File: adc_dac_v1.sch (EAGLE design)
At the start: 275 parts, among them IC1 OPA1662, IC2 ADA4610-2, IC3 ADA4610-2, IC4 OPA1662, J1 PJ-202AH, J2 PJ-002B, J3 2-406541-3, P1 M-2X06-87759_M, P2 M-2X10-87759_M, U1 AD7960BCPZ-RL7, U10 UA78M05CDCYR, U11 LP5907MFX-1.8/NOPB, U12 ADP2300AUJZ-R7, U13 LM317LIPKG3, U14 LM317LIPKG3, U15 LM337LMX/NOPB, U16 ADR395AUJZ-REEL7, U17 MAX5802, U18 LM337LMX/NOPB, U19 MAX6070BAUT21+T, U2 AD5453, U20 CD40106BM96, U21 ADA4932-1YCPZ-R7, U22 AD7960BCPZ-RL7, U23 BC857BS-13-F, U24 BC857BS-13-F, U25 ADA4932-1YCPZ-R7, U26 AD7960BCPZ-RL7, U27 ADA4932-1YCPZ-R7, U28 AD7960BCPZ-RL7, U29 AD5453, U3 ADA4932-1YCPZ-R7, U31 BC857BS-13-F, U4 NLSX3018DTR2G, U5 NLSX3018DTR2G, U6 ADS7952SRHBT, U7 OPA202, U8 REF5025AIDR, U9 ADP150AUJZ-3.3-R7, X1 BU-SMA-G, X2 BU-SMA-G, X3 BU-SMA-G, X4 BU-SMA-G, X5 BU-SMA-G, X6 BU-SMA-G, X7 BU-SMA-G, X8 BU-SMA-G, X9 1365-10

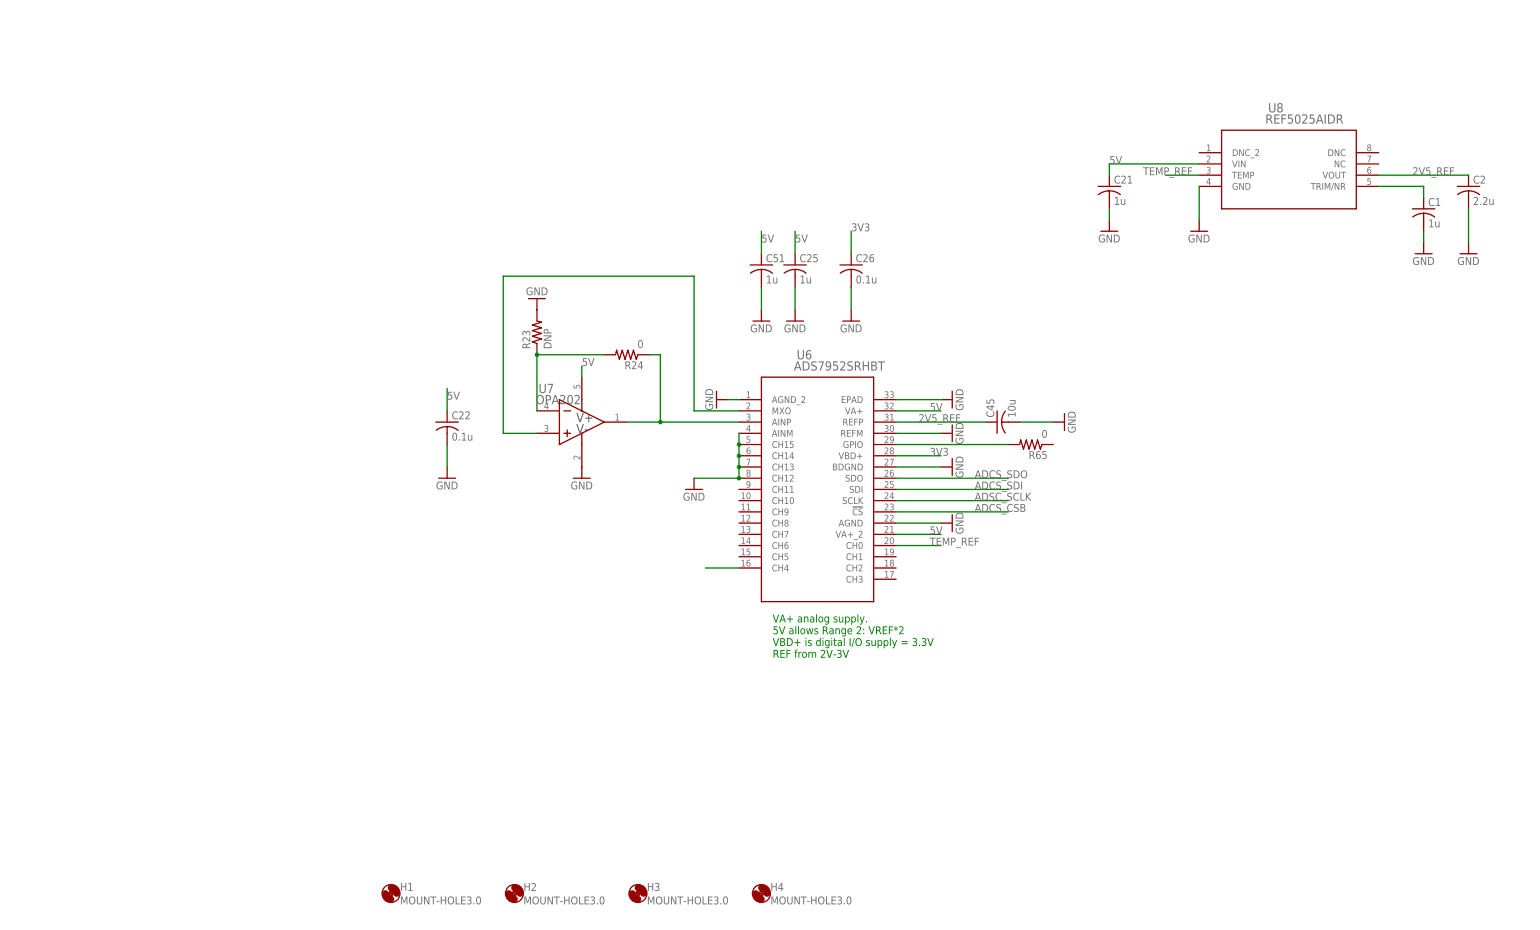
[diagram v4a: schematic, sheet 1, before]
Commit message: x4 copies of the fast DAC in layout
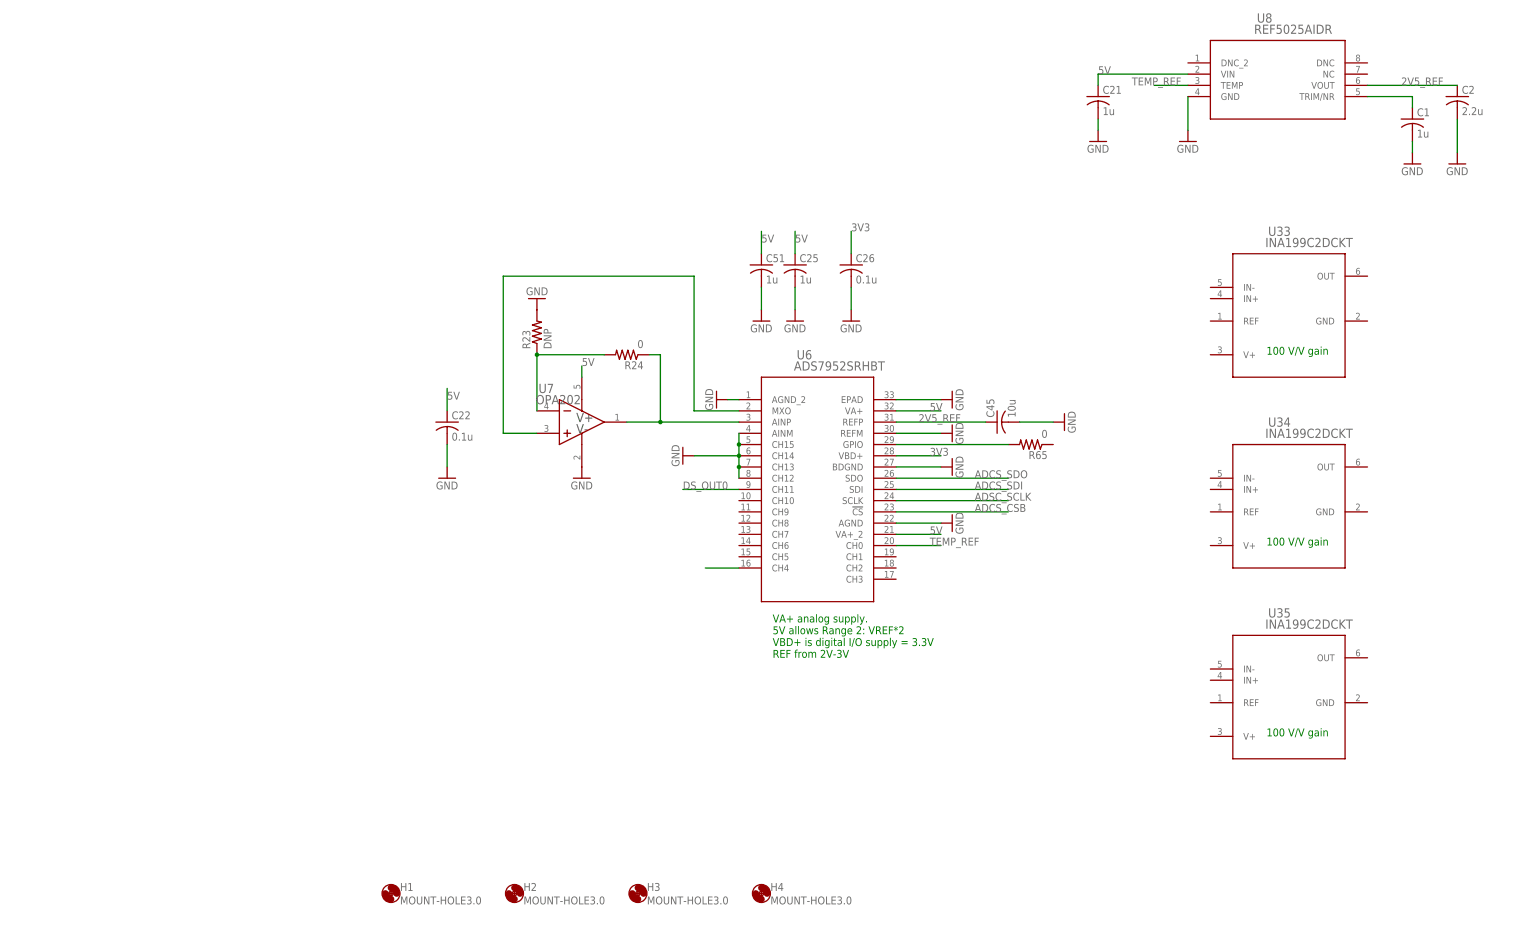
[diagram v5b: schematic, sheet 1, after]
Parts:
- added C105, C107, C113, C115: DNP, rcl:C-USC0603
- added C106, C108, C109, C111, C112, C114, C116, C117, C119, C120: 0.1u, rcl:C-USC0603
- added C110, C118: 2p, rcl:C-USC0603
- added IC5, IC7: ADA4610-2, analog-devices:ADA4692-2R
- added IC6, IC8: OPA1662, open_covg:OPA1662
- added R112, R113, R117, R122, R123, R127: 0, rcl:R-US_R0603
- added R114, R124: 10k, rcl:R-US_R0603
- added R115, R116, R125, R126: 20k, rcl:R-US_R0603
- added R118, R119, R121, R128, R129, R131: 1k, rcl:R-US_R0603
- added R120, R130: 2k, rcl:R-US_R0603
- added U30, U32: AD5453, open_covg:AD5453YRMZ-REEL7
- added U33, U34, U35: INA199C2DCKT, open_covg:INA199C2DCKT
- U29: value AD5453 -> AD5453YRMZ-REEL7
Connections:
- new net D2_CSB: U30.SYNCB
- new net D2_IOUT: C110.1, IC6B.IN+, U30.IOUT1
- new net D2_OUT: C107.1, J3.4, R113.2
- new net D2_SCLK: U30.SCLK
- new net D2_SDI: U30.SDIN
- new net D2_VREF_BUF: C105.1, R112.2, R116.1, U30.VREF
- new net D3_CSB: U32.SYNCB
- new net D3_IOUT: C118.1, IC8B.IN+, U32.IOUT1
- new net D3_OUT: C115.1, J3.7, R123.2
- new net D3_SCLK: U32.SCLK
- new net D3_SDI: U32.SDIN
- new net D3_VREF_BUF: C113.1, R122.2, R126.1, U32.VREF
- new net N$10D2: IC5B.IN-, R120.2, R121.1
- new net N$10D3: IC7B.IN-, R130.2, R131.1
- new net N$25D2: IC6A.OUT, R112.1, R118.2
- new net N$25D3: IC8A.OUT, R122.1, R128.2
- new net N$2D2: C110.2, R117.1, U30.RFB
- new net N$2D3: C118.2, R127.1, U32.RFB
- new net N$3D2: IC5A.IN+, R114.2, R115.1, R116.2
- new net N$3D3: IC7A.IN+, R124.2, R125.1, R126.2
- new net N$4D2: IC6B.OUT, R114.1, R117.2
- new net N$4D3: IC8B.OUT, R124.1, R127.2
- new net N$5D2: IC5A.OUT, IC5B.IN+, R115.2
- new net N$5D3: IC7A.OUT, IC7B.IN+, R125.2
- new net N$7D2: IC6A.IN-, R118.1, R119.2
- new net N$7D3: IC8A.IN-, R128.1, R129.2
- new net N$8D2: IC5B.OUT, R113.1, R120.1
- new net N$8D3: IC7B.OUT, R123.1, R130.1
- net +15V: now also C108.1, C112.1, C116.1, C120.1, IC5P.V+, IC6P.V+, IC7P.V+, IC8P.V+
- net -15V: now also C109.1, C111.1, C117.1, C119.1, IC5P.V-, IC6P.V-, IC7P.V-, IC8P.V-
- net 3V3: now also C106.1, C114.1, U30.VDD, U32.VDD
- net 5V_REF: now also IC6A.IN+, IC8A.IN+
- net D1_OUT: now also J3.3
- net DS_OUT0: now also U6.CH11
- net GND: now also C105.2, C106.2, C107.2, C108.2, C109.2, C111.2, C112.2, C113.2, C114.2, C115.2, C116.2, C117.2, C119.2, C120.2, IC5A.IN-, IC6B.IN-, IC7A.IN-, IC8B.IN-, J3.5, J3.6, J3.8, R119.1, R121.2, R129.1, R131.2, U30.GND, U32.GND
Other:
- note added: "100 V/V gain"
- moved on the sheet: C1, C2, C21, J3, U8

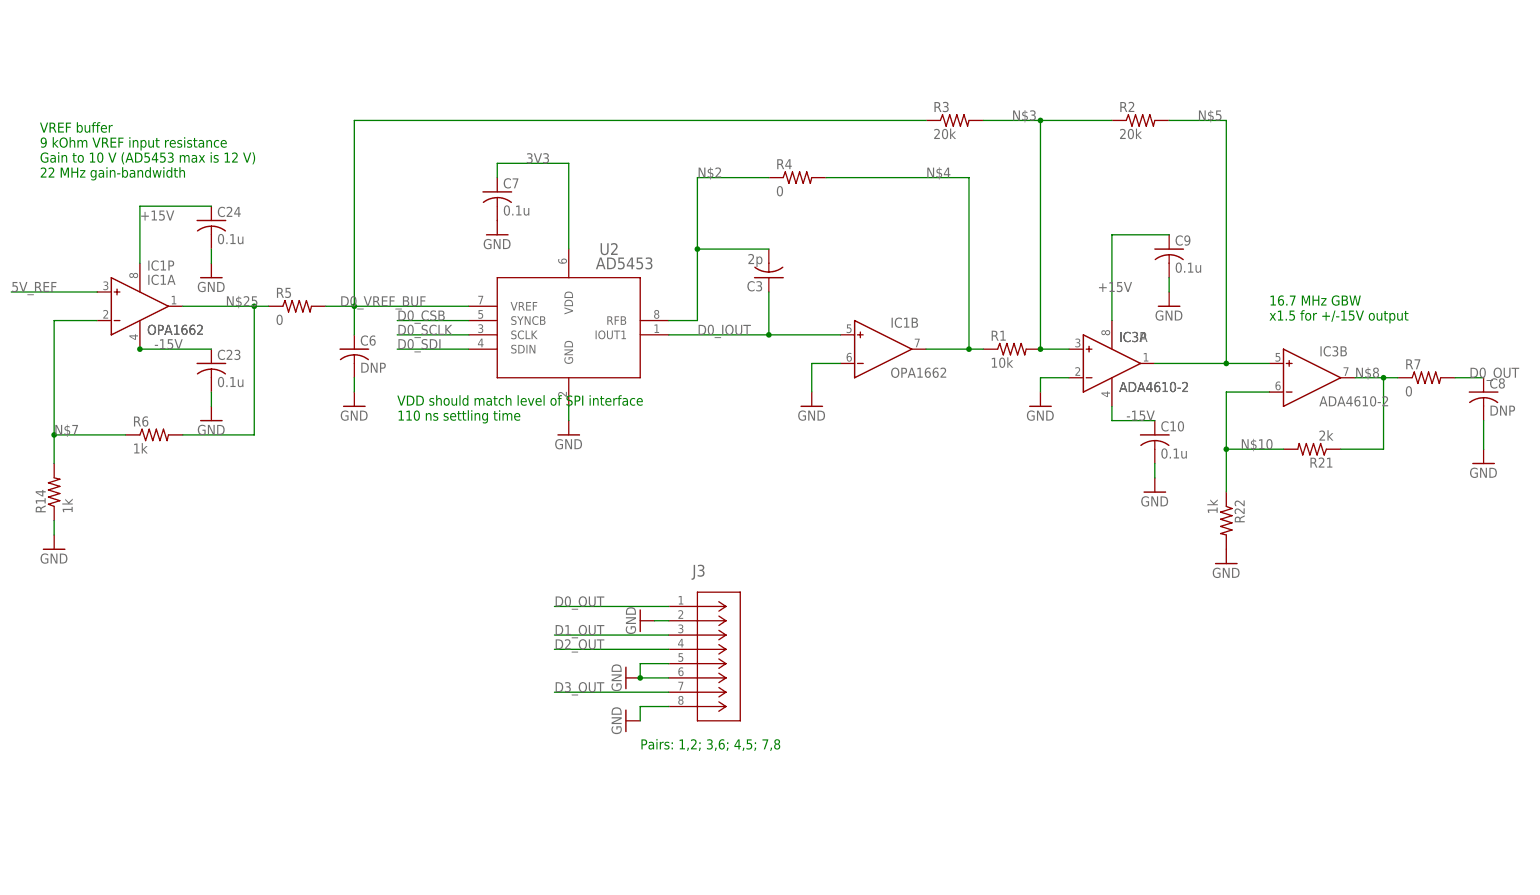
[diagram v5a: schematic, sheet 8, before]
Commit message: updated pin connection python and the pinout spreadsheet
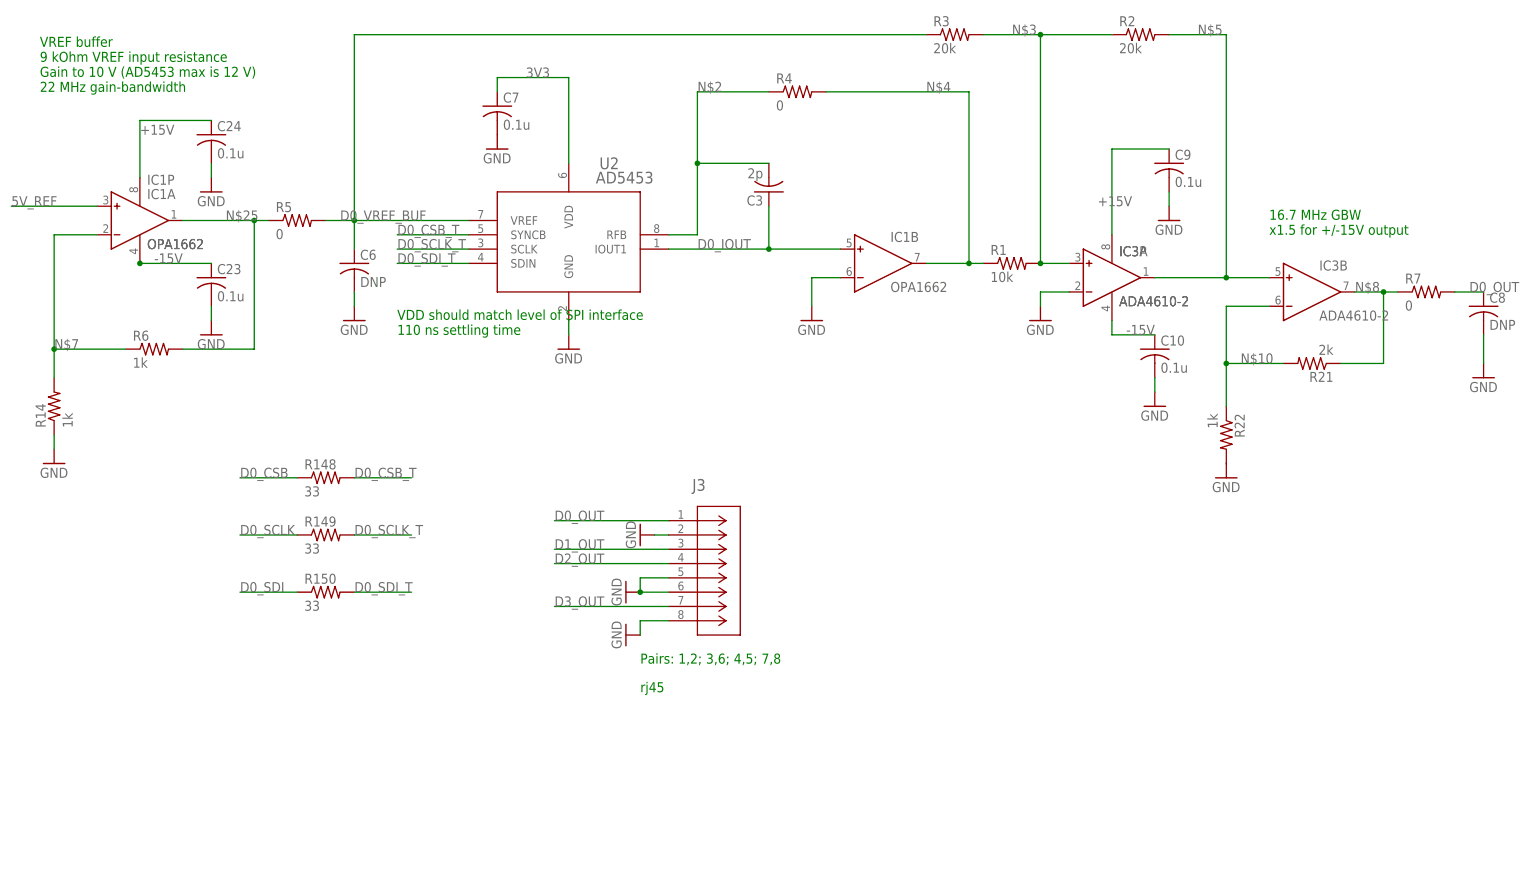
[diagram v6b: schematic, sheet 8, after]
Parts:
- removed U35: INA199C2DCKT, open_covg:INA199C2DCKT
- added C121, C122: 0.1u, rcl:C-USC0603
- added JP5: (no value), pinhead-2:PINHD-1X04_2.54-SMD
- added JP6: (no value), pinhead-2:PINHD-1X02_2.54-SMD
- added JP7: (no value), pinhead-2:PINHD-2X06_2.54-SMD
- added Q1: MMBF4117, bss138_10:MMBF4117
- added R132: 50m, rcl:R-US_R0603
- added R133: 20m, rcl:R-US_R0603
- added R134, R135, R136, R137, R138, R139, R140, R141, R142, R143, R144, R145, R146, R147, R148, R149, R150: 33, rcl:R-US_R0603
- added R151, R152: DNP, rcl:R-US_R0603
- added R153, R154: 4.7k, rcl:R-US_R0603
- added U36: AD8244BRMZ, open_covg:AD8244BRMZ
- R85, R86, R97, R98: value 0 -> DNI
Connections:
- net N$4412 renamed A2_IN_BUF-
- removed net ADSC_SCLK: U6.SCLK
- removed net JP1-10: OK1JP1_EVEN.USB_SCL
- removed net JP1-12: OK1JP1_EVEN.USB_SDA
- removed net JP1-23: OK1JP1_ODD.C5-L2P_0
- removed net JP1-25: OK1JP1_ODD.A5-L2N_0
- removed net JP1-27: OK1JP1_ODD.D14-L49P_0
- removed net JP1-29: OK1JP1_ODD.C14-L49N_0
- removed net JP1-31: OK1JP1_ODD.E16-L66P_0
- removed net JP1-32: OK1JP1_EVEN.D9-L7P_0
- removed net JP1-33: OK1JP1_ODD.D17-L66N_0
- removed net JP1-34: OK1JP1_EVEN.C8-L7N_0
- removed net JP1-37: OK1JP1_ODD.D7-L32P_0
- removed net JP1-39: OK1JP1_ODD.D8-L32N_0
- removed net JP1-46: OK1JP1_EVEN.D15-L62P_0
- removed net JP1-48: OK1JP1_EVEN.C16-L62N_0
- removed net JP1-50: OK1JP1_EVEN.B6-L4P_0
- removed net JP1-52: OK1JP1_EVEN.A6-L4N_0
- removed net JP1-54: OK1JP1_EVEN.C7-L5P_0
- removed net JP1-57: OK1JP1_ODD.A8-L6N_0
- removed net JP1-58: OK1JP1_EVEN.A7-L5N_0
- removed net JP1-59: OK1JP1_ODD.B10-L34P_0
- removed net JP1-60: OK1JP1_EVEN.C9-L8P_0
- removed net JP1-61: OK1JP1_ODD.A10-L34N_0
- removed net JP1-62: OK1JP1_EVEN.A9-L8N_0
- removed net JP1-63: OK1JP1_ODD.C13-L38P_0
- removed net JP1-64: OK1JP1_EVEN.B12-L37P_0
- removed net JP1-65: OK1JP1_ODD.A13-L38N_0
- removed net JP1-66: OK1JP1_EVEN.A12-L37N_0
- removed net JP1-67: OK1JP1_ODD.C15-L51P_0
- removed net JP1-68: OK1JP1_EVEN.B14-L50P_0
- removed net JP1-69: OK1JP1_ODD.A15-L51N_0
- removed net JP1-70: OK1JP1_EVEN.A14-L50N_0
- removed net JP1-71: OK1JP1_ODD.C17-L64P_0
- removed net JP1-72: OK1JP1_EVEN.B16-L63P_0
- removed net JP1-73: OK1JP1_ODD.A17-L64N_0
- removed net JP1-74: OK1JP1_EVEN.A16-L63N_0
- removed net JP1-75: OK1JP1_ODD.A18-L65N_0
- removed net JP1-76: OK1JP1_EVEN.B18-L65P_0
- removed net JP1-77: OK1JP1_ODD.C11-L35P_0
- removed net JP1-79: OK1JP1_ODD.A11-L35N_0
- removed net JP1-8: OK1JP1_EVEN.SYS_CLK5
- removed net JP2-11: OK1JP2_ODD.SYS_CLK4
- removed net JP2-16: OK1JP2_EVEN.G19-L33P_1
- removed net JP2-17: OK1JP2_ODD.G17-L9N_1
- removed net JP2-18: OK1JP2_EVEN.F20-L33N_1
- removed net JP2-19: OK1JP2_ODD.H19-L34P_1
- removed net JP2-20: OK1JP2_EVEN.H20-L38P_1
- removed net JP2-21: OK1JP2_ODD.H18-L34N_1
- removed net JP2-22: OK1JP2_EVEN.J19-L38N_1
- removed net JP2-23: OK1JP2_ODD.F16-L10P_1
- removed net JP2-24: OK1JP2_EVEN.D19-L29P_1
- removed net JP2-25: OK1JP2_ODD.F17-L10N_1
- removed net JP2-27: OK1JP2_ODD.J17-L36P_1
- removed net JP2-28: OK1JP2_EVEN.F18-L30P_1
- removed net JP2-29: OK1JP2_ODD.K17-L36N_1
- removed net JP2-30: OK1JP2_EVEN.F19-L30N_1
- removed net JP2-31: OK1JP2_ODD.K16-L21P_1
- removed net JP2-32: OK1JP2_EVEN.M16-L58P_1
- removed net JP2-33: OK1JP2_ODD.J16-L21N_1
- removed net JP2-37: OK1JP2_ODD.V21-L52P_1
- removed net JP2-39: OK1JP2_ODD.V22-L52N_1
- removed net JP2-41: OK1JP2_ODD.T21-L50P_1
- removed net JP2-43: OK1JP2_ODD.T22-L50N_1
- removed net JP2-45: OK1JP2_ODD.P21-L48P_1
- removed net JP2-47: OK1JP2_ODD.P22-L48N_1
- removed net JP2-49: OK1JP2_ODD.M21-L46P_1
- removed net JP2-51: OK1JP2_ODD.M22-L46N_1
- removed net JP2-57: OK1JP2_ODD.L22-L45N_1
- removed net JP2-58: OK1JP2_EVEN.L19-L42N_1
- removed net JP2-59: OK1JP2_ODD.H21-L41P_1
- removed net JP2-60: OK1JP2_EVEN.K21-L44P_1
- removed net JP2-61: OK1JP2_ODD.H22-L41N_1
- removed net JP2-62: OK1JP2_EVEN.K22-L44N_1
- removed net JP2-63: OK1JP2_ODD.F21-L37P_1
- removed net JP2-64: OK1JP2_EVEN.G20-L39P_1
- removed net JP2-65: OK1JP2_ODD.F22-L37N_1
- removed net JP2-66: OK1JP2_EVEN.G22-L39N_1
- removed net JP2-67: OK1JP2_ODD.D21-L31P_1
- removed net JP2-68: OK1JP2_EVEN.E20-L35P_1
- removed net JP2-69: OK1JP2_ODD.D22-L31N_1
- removed net JP2-70: OK1JP2_EVEN.E22-L35N_1
- removed net JP2-71: OK1JP2_ODD.B21-L19P_1
- removed net JP2-72: OK1JP2_EVEN.C20-L32P_1
- removed net JP2-73: OK1JP2_ODD.B22-L19N-1
- removed net N$4212: C77.1, R80.1, R85.2, R87.1
- removed net N$4213: C91.1, R92.1, R97.2, R99.1
- removed net N$4413: C90.1, R93.1, R96.2, R98.2
- new net 5V_ISENSE: U34.OUT, U6.CH2
- new net 5V_SENSE: C33.1, R133.1, U10.OUT, U34.IN+
- new net A2_IN+_BUF: C77.1, R80.1, R85.2, R87.1, U36.OUTC
- new net A2_IN-_BUF: U36.OUTD
- new net A3_IN+_BUF: C91.1, R92.1, R97.2, R99.1, U36.OUTA
- new net A3_IN-_BUF: C90.1, R93.1, R96.2, R98.2, U36.OUTB
- new net ADCS_SCLK: OK1JP2_EVEN.H20-L38P_1, R136.1
- new net D0_CSB_T: R148.2, U2.SYNCB
- new net D0_SCLK_T: R149.2, U2.SCLK
- new net D0_SDI_T: R150.2, U2.SDIN
- new net D1_CSB_T: U29.SYNCB
- new net D1_SCLK_T: R140.2, U29.SCLK
- new net D1_SDI_T: R141.2, U29.SDIN
- new net D2_CSB_T: R142.2, U30.SYNCB
- new net D2_SCLK_T: R143.2, U30.SCLK
- new net D2_SDI_T: R144.2, U30.SDIN
- new net D3_CSB_T: R145.2, U32.SYNCB
- new net D3_SCLK_T: R146.2, U32.SCLK
- new net D3_SDI_T: R147.2, U32.SDIN
- new net GP_0: OK1JP2_EVEN.K21-L44P_1, P2.7
- new net GP_1: OK1JP2_ODD.H22-L41N_1, P2.9
- new net GP_10: OK1JP2_EVEN.E22-L35N_1, P2.10
- new net GP_11: OK1JP2_ODD.B21-L19P_1, P2.12
- new net GP_2: OK1JP2_EVEN.K22-L44N_1, P2.11
- new net GP_3: OK1JP2_ODD.F21-L37P_1, P2.13
- new net GP_4: OK1JP2_EVEN.G20-L39P_1, P2.15
- new net GP_5: OK1JP2_ODD.F22-L37N_1, P2.17
- new net GP_6: OK1JP2_EVEN.G22-L39N_1, P2.2
- new net GP_7: OK1JP2_ODD.D21-L31P_1, P2.4
- new net GP_8: OK1JP2_EVEN.E20-L35P_1, P2.6
- new net GP_9: OK1JP2_ODD.D22-L31N_1, P2.8
- new net GP_ADC10: JP7.1, U6.CH10
- new net GP_ADC3: U6.CH3
- new net GP_ADC4: JP7.8, U6.CH4
- new net GP_ADC5: JP7.10, U6.CH5
- new net GP_ADC6: JP7.9, U6.CH6
- new net GP_ADC7: JP7.7, U6.CH7
- new net GP_ADC8: JP7.5, U6.CH8
- new net GP_ADC9: JP7.3, U6.CH9
- new net GP_ISENSE: U33.OUT, U6.CH1
- new net GP_SCL: OK1JP2_ODD.B22-L19N-1, P2.16, R154.1
- new net GP_SDA: OK1JP2_EVEN.C20-L32P_1, P2.14, R153.1
- new net I_SENSE+: JP5.3, R132.1, U33.IN+
- new net I_SENSE-: JP5.1, R132.2, U33.IN-
- new net JP2-12: OK1JP2_EVEN.NC_12
- new net JP2-3: OK1JP2_ODD.NC_3
- new net N$1: JP6.2, Q1.S
- new net N$50: JP6.1, Q1.D
- new net N$51: R136.2, U6.SCLK
- new net N$52: R65.1
- new net N$53: R137.2, U6.SDI
- new net N$54: R139.2
- net 3V3: now also R153.2, R154.2
- net 5V: now also R133.2, U33.V+, U34.IN-, U34.V+; no longer C33.1, U10.OUT
- net A0_CLK+: now also OK1JP1_ODD.D7-L32P_0
- net A0_CLK-: now also OK1JP1_ODD.D8-L32N_0
- net A0_CNV+: now also OK1JP1_ODD.C5-L2P_0
- net A0_CNV-: now also OK1JP1_ODD.A5-L2N_0
- net A0_D+: now also OK1JP1_ODD.D14-L49P_0
- net A0_D-: now also OK1JP1_ODD.C14-L49N_0
- net A0_DCO+: now also OK1JP1_ODD.E16-L66P_0
- net A0_DCO-: now also OK1JP1_ODD.D17-L66N_0
- net A0_EN0: now also OK1JP1_EVEN.D9-L7P_0
- net A1_CLK+: now also OK1JP1_ODD.B10-L34P_0
- net A1_CLK-: now also OK1JP1_ODD.A10-L34N_0
- net A1_CNV+: now also OK1JP1_EVEN.D15-L62P_0
- net A1_CNV-: now also OK1JP1_EVEN.C16-L62N_0
- net A1_D+: now also OK1JP1_EVEN.B6-L4P_0
- net A1_D-: now also OK1JP1_EVEN.A6-L4N_0
- net A1_DCO+: now also OK1JP1_EVEN.C7-L5P_0
- net A1_DCO-: now also OK1JP1_EVEN.A7-L5N_0
- net A1_EN0: now also OK1JP1_ODD.A8-L6N_0
- net A2_AMP_IN+: now also U36.INC
- net A2_AMP_IN-: now also U36.IND
- net A2_CLK+: now also OK1JP1_EVEN.B18-L65P_0
- net A2_CLK-: now also OK1JP1_ODD.A18-L65N_0
- net A2_CNV+: now also OK1JP1_ODD.C13-L38P_0
- net A2_CNV-: now also OK1JP1_ODD.A13-L38N_0
- net A2_D+: now also OK1JP1_ODD.C15-L51P_0
- net A2_D-: now also OK1JP1_ODD.A15-L51N_0
- net A2_DCO+: now also OK1JP1_ODD.C17-L64P_0
- net A2_DCO-: now also OK1JP1_ODD.A17-L64N_0
- net A2_EN0: now also OK1JP1_EVEN.B16-L63P_0
- net A3_AMP_IN+: now also U36.INA
- net A3_AMP_IN-: now also U36.INB
- net A3_CLK+: now also OK1JP1_ODD.C11-L35P_0
- net A3_CLK-: now also OK1JP1_ODD.A11-L35N_0
- net A3_CNV+: now also OK1JP1_EVEN.C9-L8P_0
- net A3_CNV-: now also OK1JP1_EVEN.A9-L8N_0
- net A3_D+: now also OK1JP1_EVEN.B12-L37P_0
- net A3_D-: now also OK1JP1_EVEN.A12-L37N_0
- net A3_DCO+: now also OK1JP1_EVEN.B14-L50P_0
- net A3_DCO-: now also OK1JP1_EVEN.A14-L50N_0
- net A3_EN0: now also OK1JP1_EVEN.A16-L63N_0
- net ADCS_CSB: now also OK1JP2_EVEN.J19-L38N_1, R135.1; no longer U6.!CS
- net ADCS_SDI: now also OK1JP2_EVEN.F20-L33N_1, R137.1; no longer U6.SDI
- net ADCS_SDO: now also OK1JP2_EVEN.G19-L33P_1, R134.1, R134.2
- net AMP_PWR+: now also C121.1, U36.+VS
- net AMP_PWR-: now also C122.1, U36.-VS
- net A_EN1: now also OK1JP1_EVEN.USB_SDA
- net A_EN2_HV: now also OK1JP1_EVEN.C8-L7N_0
- net A_EN3: now also OK1JP2_ODD.SYS_CLK4
- net D0_CSB: now also OK1JP2_ODD.T21-L50P_1, P2.1, R148.1; no longer U2.SYNCB
- net D0_SCLK: now also OK1JP2_ODD.P21-L48P_1, P2.5, R149.1; no longer U2.SCLK
- net D0_SDI: now also OK1JP2_ODD.T22-L50N_1, P2.3, R150.1; no longer U2.SDIN
- net D1_CSB: now also OK1JP2_ODD.P22-L48N_1, R139.1; no longer U29.SYNCB
- net D1_SCLK: now also OK1JP2_ODD.M22-L46N_1, R140.1; no longer U29.SCLK
- net D1_SDI: now also OK1JP2_ODD.M21-L46P_1, R141.1; no longer U29.SDIN
- net D2_CSB: now also OK1JP2_ODD.J16-L21N_1, R142.1; no longer U30.SYNCB
- net D2_SCLK: now also OK1JP2_ODD.V22-L52N_1, R143.1; no longer U30.SCLK
- net D2_SDI: now also OK1JP2_ODD.V21-L52P_1, R144.1; no longer U30.SDIN
- net D3_CSB: now also OK1JP2_ODD.J17-L36P_1, R145.1; no longer U32.SYNCB
- net D3_SCLK: now also OK1JP2_ODD.K16-L21P_1, R146.1; no longer U32.SCLK
- net D3_SDI: now also OK1JP2_ODD.K17-L36N_1, R147.1; no longer U32.SDIN
- net DS_CLRB: now also OK1JP2_EVEN.M16-L58P_1
- net DS_OUT0: now also JP7.2
- net DS_OUT1: now also JP7.4
- net DS_SCL: now also OK1JP2_EVEN.F19-L30N_1
- net DS_SDA: now also OK1JP2_EVEN.F18-L30P_1
- net GND: now also C121.2, C122.2, JP5.2, JP5.4, JP7.11, JP7.12, JP7.6, P2.18, P2.19, P2.20, U33.GND, U33.REF, U34.GND, U34.REF
- net GPIO_3V3_0: now also OK1JP2_ODD.L22-L45N_1
- net GPIO_3V3_1: now also OK1JP2_EVEN.L19-L42N_1
- net GPIO_3V3_2: now also OK1JP2_ODD.H21-L41P_1
- net LS0_EN: now also OK1JP1_EVEN.SYS_CLK5
- net LS1_EN: now also OK1JP1_EVEN.USB_SCL
- net LS_IN0: now also OK1JP2_ODD.G17-L9N_1
- net LS_IN1: now also OK1JP2_ODD.H19-L34P_1
- net LS_IN2: now also OK1JP2_ODD.H18-L34N_1
- net LS_IN3: now also OK1JP2_ODD.F16-L10P_1
- net LS_IN4: now also OK1JP2_EVEN.D19-L29P_1
- net LS_IN5: now also OK1JP2_ODD.F17-L10N_1
- net LS_OUT5: now also Q1.G
- net N$23: now also R135.2, U6.!CS; no longer U6.CH4
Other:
- note added: "rj45"
- moved on the sheet: C10, C23, C24, C3, C49, C50, C6, C7, C8, C9, IC1A, IC1B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
